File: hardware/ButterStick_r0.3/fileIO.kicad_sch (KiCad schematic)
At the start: 2 parts, among them J4 MicroSD, U20 PUSB3FR6

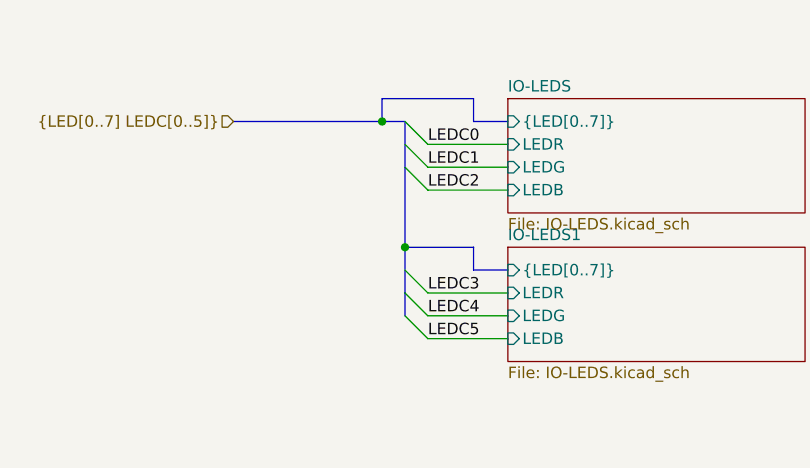
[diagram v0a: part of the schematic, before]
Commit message: hw.r0_3: routing improvements
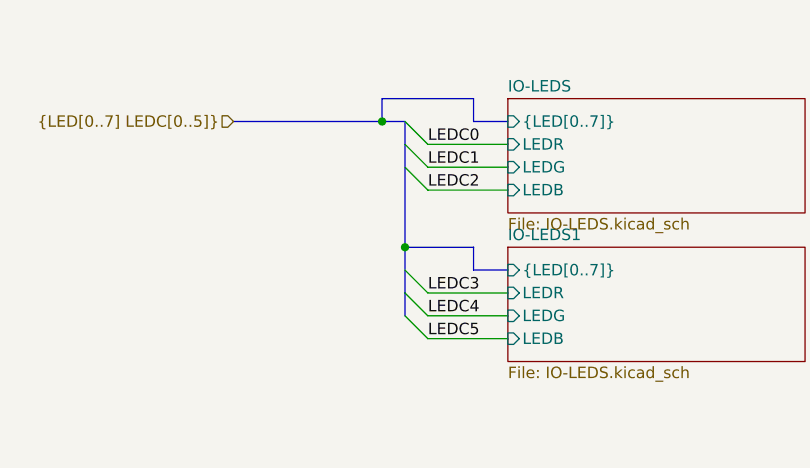
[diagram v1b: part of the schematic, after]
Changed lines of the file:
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@@
 (kicad_sch (version 20200512) (host eeschema "5.99.0-unknown-c8476d6~101~ubuntu18.04.1")
-  (page 4 20)
+  (page 1 20)
   (paper "A4")
   (title_block
@@
   (bus (pts (xy 76.2 40.64) (xy 76.2 38.1)))
   (bus (pts (xy 76.2 40.64) (xy 78.74 40.64)))
-  (bus (pts (xy 78.74 40.64) (xy 78.74 45.72)))
-  (bus (pts (xy 78.74 45.72) (xy 78.74 54.61)))
+  (bus (pts (xy 78.74 40.64) (xy 78.74 43.18)))
+  (bus (pts (xy 78.74 43.18) (xy 78.74 54.61)))
   (bus (pts (xy 78.74 54.61) (xy 78.74 59.69)))
   (bus (pts (xy 78.74 59.69) (xy 78.74 62.23)))

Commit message: hw.r0_3: Start routing DDR3 interface
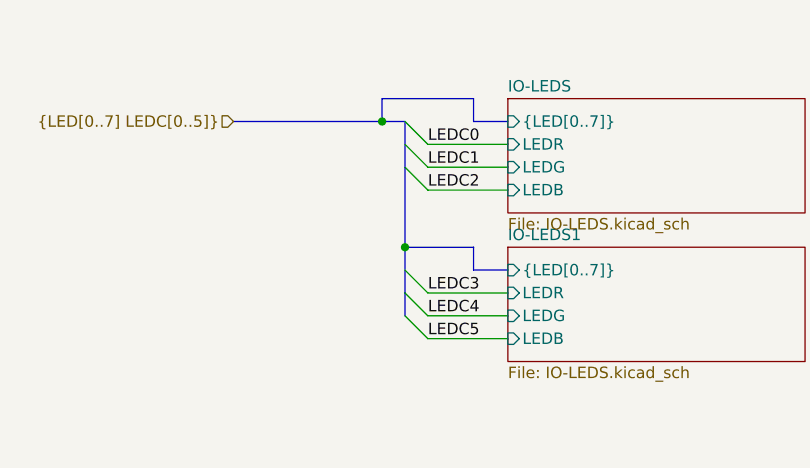
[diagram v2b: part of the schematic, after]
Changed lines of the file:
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@@
-(kicad_sch (version 20200512) (host eeschema "5.99.0-unknown-c8476d6~101~ubuntu18.04.1")
+(kicad_sch (version 20200512) (host eeschema "5.99.0-unknown-711fc99~101~ubuntu18.04.1")
   (page 1 20)
   (paper "A4")
@@
   (bus (pts (xy 76.2 40.64) (xy 76.2 38.1)))
   (bus (pts (xy 76.2 40.64) (xy 78.74 40.64)))
-  (bus (pts (xy 78.74 40.64) (xy 78.74 43.18)))
-  (bus (pts (xy 78.74 43.18) (xy 78.74 54.61)))
+  (bus (pts (xy 78.74 40.64) (xy 78.74 45.72)))
+  (bus (pts (xy 78.74 45.72) (xy 78.74 54.61)))
   (bus (pts (xy 78.74 54.61) (xy 78.74 59.69)))
   (bus (pts (xy 78.74 59.69) (xy 78.74 62.23)))

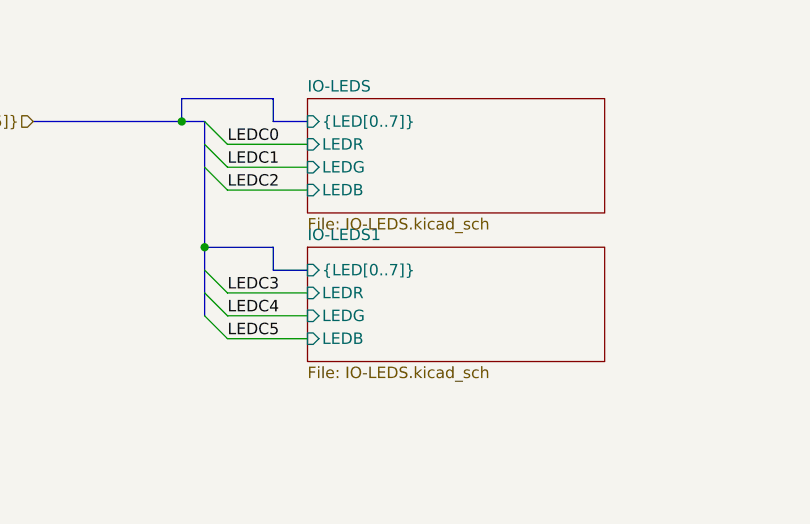
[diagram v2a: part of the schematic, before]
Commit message: hw.r0_3: Inital routing of DDR3 done
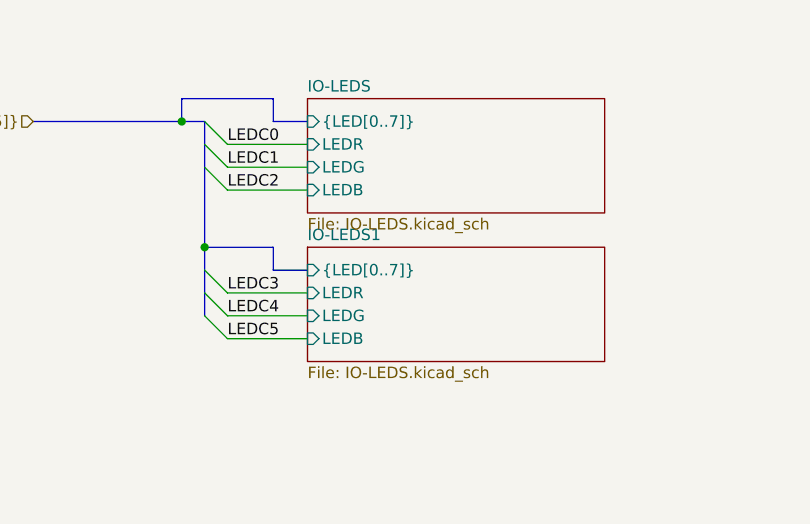
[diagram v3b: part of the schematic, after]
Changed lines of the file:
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@@
   (bus (pts (xy 76.2 40.64) (xy 76.2 38.1)))
   (bus (pts (xy 76.2 40.64) (xy 78.74 40.64)))
-  (bus (pts (xy 78.74 40.64) (xy 78.74 45.72)))
-  (bus (pts (xy 78.74 45.72) (xy 78.74 54.61)))
+  (bus (pts (xy 78.74 40.64) (xy 78.74 43.18)))
+  (bus (pts (xy 78.74 43.18) (xy 78.74 54.61)))
   (bus (pts (xy 78.74 54.61) (xy 78.74 59.69)))
   (bus (pts (xy 78.74 59.69) (xy 78.74 62.23)))
@@
   )
   (sheet (at 90.17 38.1) (size 33.02 12.7)
+    (stroke (width 0.1524) (color 132 0 132 1))
+    (fill (color 255 255 255 1.0000))
     (property "Sheet name" "IO-LEDS" (id 0) (at 90.17 37.4645 0)
       (effects (font (size 1.27 1.27)) (justify left bottom))
@@
   )
   (sheet (at 90.17 54.61) (size 33.02 12.7)
+    (stroke (width 0.1524) (color 132 0 132 1))
+    (fill (color 255 255 255 1.0000))
     (property "Sheet name" "IO-LEDS1" (id 0) (at 90.17 53.9745 0)
       (effects (font (size 1.27 1.27)) (justify left bottom))

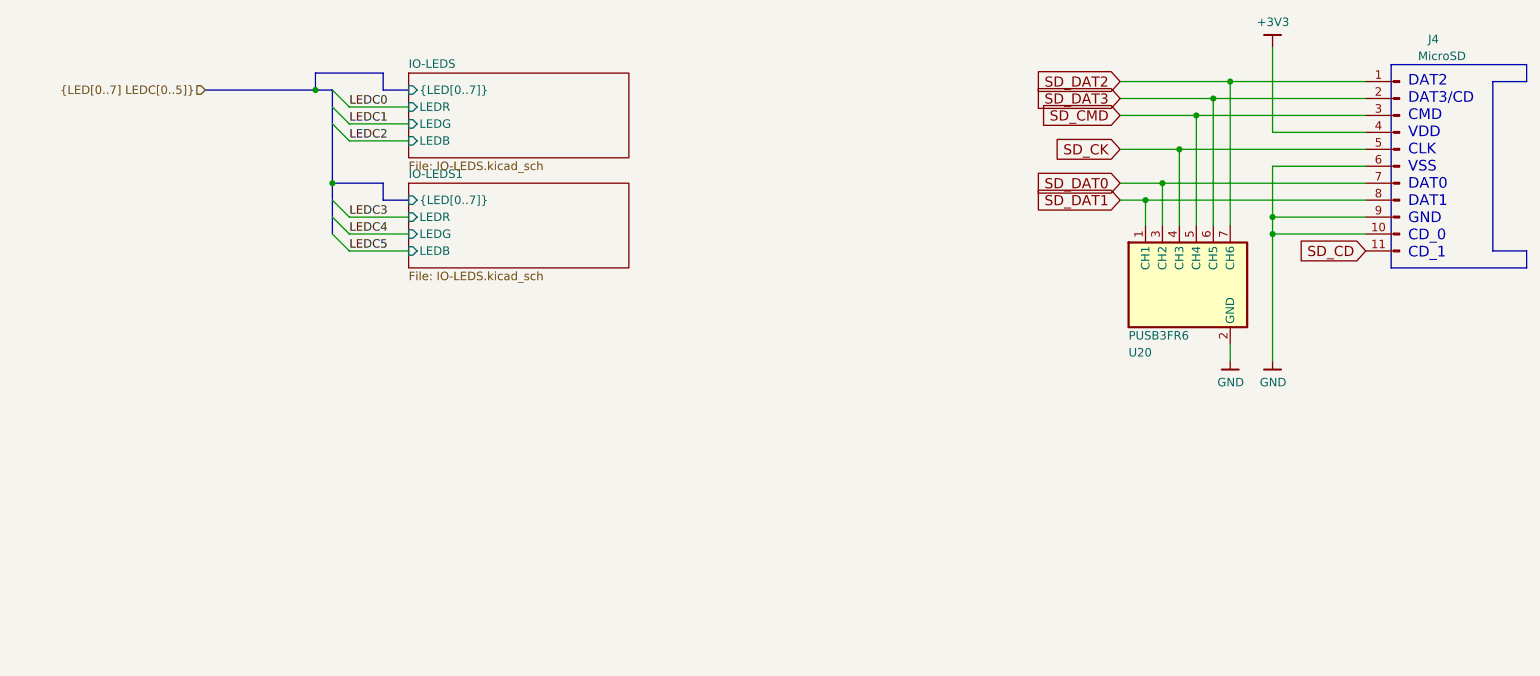
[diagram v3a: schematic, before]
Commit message: hw.r0_3: routed SYZYGY, begin routing RGMII/ULPI
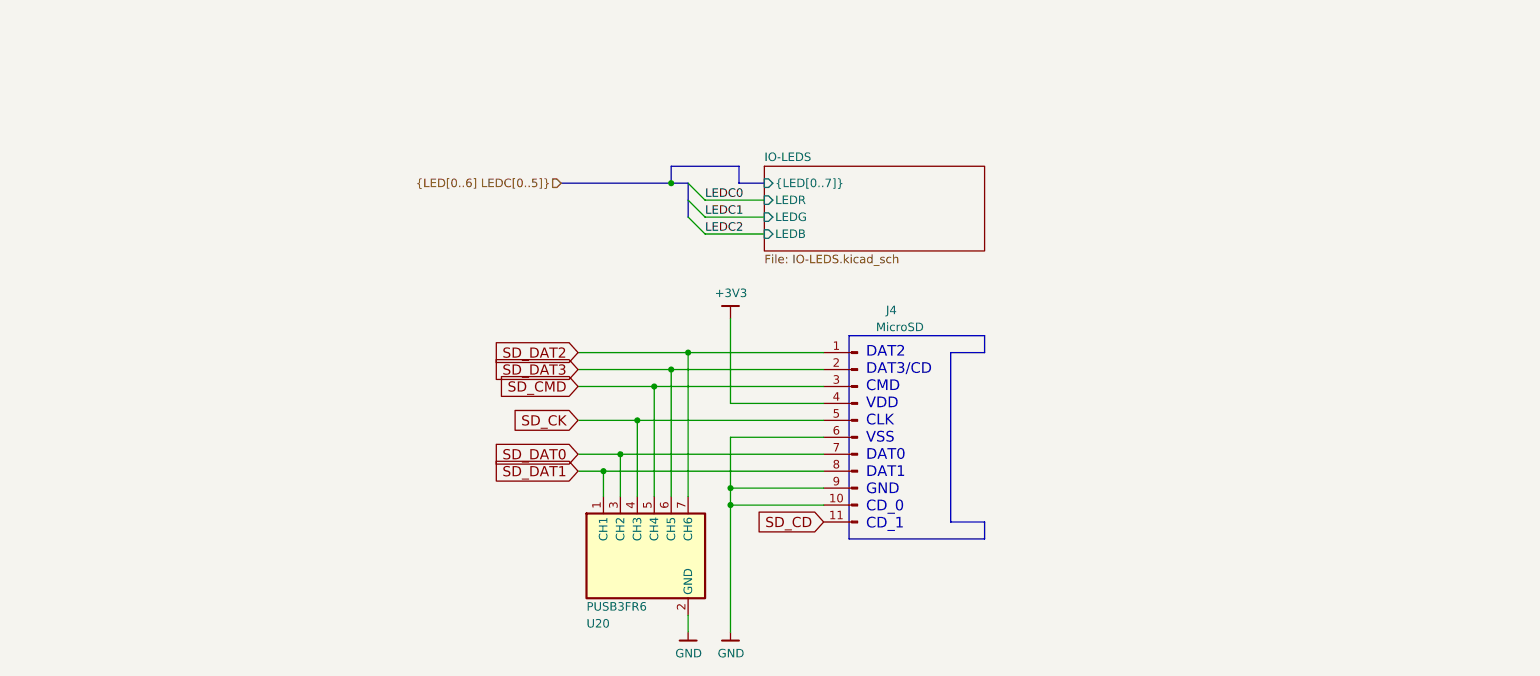
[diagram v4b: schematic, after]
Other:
- removed sheet IO-LEDS1
- moved on the sheet: J4, U20

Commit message: hw.r0_3: major blocks roughly routed
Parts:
- renumbered J4 to J2, U20 to U3
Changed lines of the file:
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@@
   )
   (symbol (lib_id "gkl_power:GND") (at 132.08 121.92 0) (unit 1)
-    (property "Reference" "#PWR0258" (id 0) (at 132.08 128.27 0)
+    (property "Reference" "#PWR054" (id 0) (at 132.08 128.27 0)
       (effects (font (size 1.27 1.27)) hide)
     )
@@
   )
   (symbol (lib_id "gkl_power:GND") (at 138.43 121.92 0) (unit 1)
-    (property "Reference" "#PWR0257" (id 0) (at 138.43 128.27 0)
+    (property "Reference" "#PWR056" (id 0) (at 138.43 128.27 0)
       (effects (font (size 1.27 1.27)) hide)
     )
@@
   )
   (symbol (lib_id "gkl_power:+3V3") (at 138.43 74.93 0) (unit 1)
-    (property "Reference" "#PWR0256" (id 0) (at 138.43 78.74 0)
+    (property "Reference" "#PWR055" (id 0) (at 138.43 78.74 0)
       (effects (font (size 1.27 1.27)) hide)
     )
@@
   )
   (symbol (lib_id "Connector:Conn_01x11_Male") (at 157.48 92.71 0) (mirror y) (unit 1)
-    (property "Reference" "J4" (id 0) (at 162.56 73.66 0))
+    (property "Reference" "J2" (id 0) (at 162.56 73.66 0))
     (property "Value" "MicroSD" (id 1) (at 163.83 76.2 0))
     (property "Footprint" "gkl_conn:molex_microsd_1040310811" (id 2) (at 157.48 92.71 0)
@@
   )
   (symbol (lib_id "gkl_misc:PUSB3FR6") (at 125.73 110.49 90) (mirror x) (unit 1)
-    (property "Reference" "U20" (id 0) (at 116.84 120.65 90)
+    (property "Reference" "U3" (id 0) (at 116.84 120.65 90)
       (effects (font (size 1.27 1.27)) (justify right))
     )

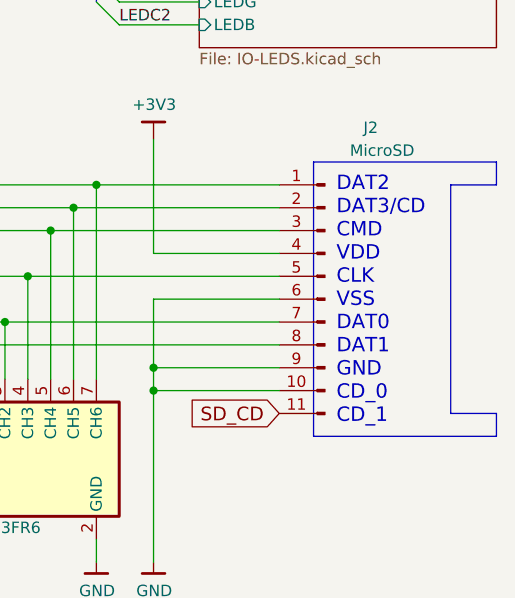
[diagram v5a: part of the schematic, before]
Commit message: hw.r0d3: Length matched all SYZYGY ports
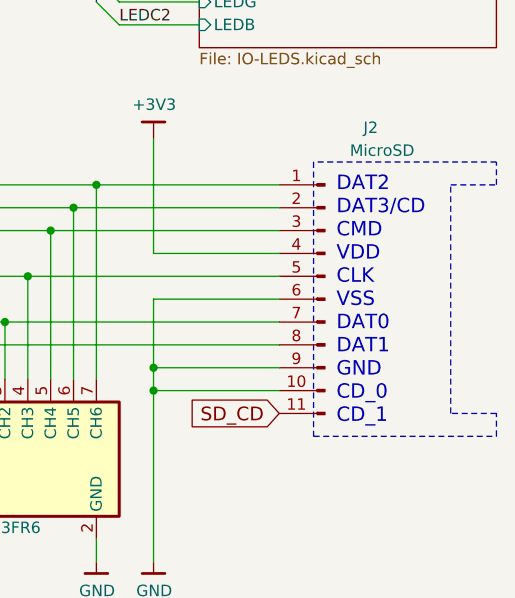
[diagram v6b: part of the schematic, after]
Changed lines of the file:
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@@
-(kicad_sch (version 20200512) (host eeschema "5.99.0-unknown-711fc99~101~ubuntu18.04.1")
+(kicad_sch (version 20200608) (host eeschema "5.99.0-unknown-08c61e6~101~ubuntu18.04.1")
   (page 1 19)
   (paper "A4")
@@
   (bus_entry (at 134.62 59.69) (size -2.54 -2.54))
   (bus_entry (at 134.62 62.23) (size -2.54 -2.54))
-  (wire (pts (xy 115.57 80.01) (xy 132.08 80.01)))
-  (wire (pts (xy 115.57 82.55) (xy 129.54 82.55)))
-  (wire (pts (xy 115.57 85.09) (xy 127 85.09)))
-  (wire (pts (xy 115.57 90.17) (xy 124.46 90.17)))
-  (wire (pts (xy 115.57 95.25) (xy 121.92 95.25)))
-  (wire (pts (xy 115.57 97.79) (xy 119.38 97.79)))
-  (wire (pts (xy 119.38 97.79) (xy 152.4 97.79)))
-  (wire (pts (xy 119.38 101.6) (xy 119.38 97.79)))
-  (wire (pts (xy 121.92 95.25) (xy 152.4 95.25)))
-  (wire (pts (xy 121.92 101.6) (xy 121.92 95.25)))
-  (wire (pts (xy 124.46 90.17) (xy 152.4 90.17)))
-  (wire (pts (xy 124.46 101.6) (xy 124.46 90.17)))
-  (wire (pts (xy 127 85.09) (xy 152.4 85.09)))
-  (wire (pts (xy 127 101.6) (xy 127 85.09)))
-  (wire (pts (xy 129.54 82.55) (xy 152.4 82.55)))
-  (wire (pts (xy 129.54 101.6) (xy 129.54 82.55)))
-  (wire (pts (xy 132.08 80.01) (xy 152.4 80.01)))
-  (wire (pts (xy 132.08 101.6) (xy 132.08 80.01)))
-  (wire (pts (xy 132.08 119.38) (xy 132.08 121.92)))
-  (wire (pts (xy 134.62 57.15) (xy 143.51 57.15)))
-  (wire (pts (xy 134.62 59.69) (xy 143.51 59.69)))
-  (wire (pts (xy 134.62 62.23) (xy 143.51 62.23)))
-  (wire (pts (xy 138.43 87.63) (xy 138.43 74.93)))
-  (wire (pts (xy 138.43 92.71) (xy 138.43 100.33)))
-  (wire (pts (xy 138.43 100.33) (xy 138.43 102.87)))
-  (wire (pts (xy 138.43 100.33) (xy 152.4 100.33)))
-  (wire (pts (xy 138.43 102.87) (xy 138.43 121.92)))
-  (wire (pts (xy 152.4 87.63) (xy 138.43 87.63)))
-  (wire (pts (xy 152.4 92.71) (xy 138.43 92.71)))
-  (wire (pts (xy 152.4 102.87) (xy 138.43 102.87)))
-  (bus (pts (xy 113.03 54.61) (xy 129.54 54.61)))
-  (bus (pts (xy 129.54 52.07) (xy 139.7 52.07)))
-  (bus (pts (xy 129.54 54.61) (xy 129.54 52.07)))
-  (bus (pts (xy 129.54 54.61) (xy 132.08 54.61)))
-  (bus (pts (xy 132.08 54.61) (xy 132.08 59.69)))
-  (bus (pts (xy 139.7 52.07) (xy 139.7 54.61)))
-  (bus (pts (xy 139.7 54.61) (xy 143.51 54.61)))
-  (polyline (pts (xy 156.21 77.47) (xy 156.21 107.95)))
-  (polyline (pts (xy 156.21 107.95) (xy 176.53 107.95)))
-  (polyline (pts (xy 171.45 80.01) (xy 176.53 80.01)))
-  (polyline (pts (xy 171.45 105.41) (xy 171.45 80.01)))
-  (polyline (pts (xy 176.53 77.47) (xy 156.21 77.47)))
-  (polyline (pts (xy 176.53 80.01) (xy 176.53 77.47)))
-  (polyline (pts (xy 176.53 105.41) (xy 171.45 105.41)))
-  (polyline (pts (xy 176.53 107.95) (xy 176.53 105.41)))
+  (wire (pts (xy 115.57 80.01) (xy 132.08 80.01))
+    (stroke (width 0) (type solid) (color 0 0 0 0))
+  )
+  (wire (pts (xy 115.57 82.55) (xy 129.54 82.55))
+    (stroke (width 0) (type solid) (color 0 0 0 0))
+  )
+  (wire (pts (xy 115.57 85.09) (xy 127 85.09))
+    (stroke (width 0) (type solid) (color 0 0 0 0))
+  )
+  (wire (pts (xy 115.57 90.17) (xy 124.46 90.17))
+    (stroke (width 0) (type solid) (color 0 0 0 0))
+  )
+  (wire (pts (xy 115.57 95.25) (xy 121.92 95.25))
+    (stroke (width 0) (type solid) (color 0 0 0 0))
+  )
+  (wire (pts (xy 115.57 97.79) (xy 119.38 97.79))
+    (stroke (width 0) (type solid) (color 0 0 0 0))
+  )
+  (wire (pts (xy 119.38 97.79) (xy 152.4 97.79))
+    (stroke (width 0) (type solid) (color 0 0 0 0))
+  )
+  (wire (pts (xy 119.38 101.6) (xy 119.38 97.79))
+    (stroke (width 0) (type solid) (color 0 0 0 0))
+  )
+  (wire (pts (xy 121.92 95.25) (xy 152.4 95.25))
+    (stroke (width 0) (type solid) (color 0 0 0 0))
+  )
+  (wire (pts (xy 121.92 101.6) (xy 121.92 95.25))
+    (stroke (width 0) (type solid) (color 0 0 0 0))
+  )
+  (wire (pts (xy 124.46 90.17) (xy 152.4 90.17))
+    (stroke (width 0) (type solid) (color 0 0 0 0))
+  )
+  (wire (pts (xy 124.46 101.6) (xy 124.46 90.17))
+    (stroke (width 0) (type solid) (color 0 0 0 0))
+  )
+  (wire (pts (xy 127 85.09) (xy 152.4 85.09))
+    (stroke (width 0) (type solid) (color 0 0 0 0))
+  )
+  (wire (pts (xy 127 101.6) (xy 127 85.09))
+    (stroke (width 0) (type solid) (color 0 0 0 0))
+  )
+  (wire (pts (xy 129.54 82.55) (xy 152.4 82.55))
+    (stroke (width 0) (type solid) (color 0 0 0 0))
+  )
+  (wire (pts (xy 129.54 101.6) (xy 129.54 82.55))
+    (stroke (width 0) (type solid) (color 0 0 0 0))
+  )
+  (wire (pts (xy 132.08 80.01) (xy 152.4 80.01))
+    (stroke (width 0) (type solid) (color 0 0 0 0))
+  )
+  (wire (pts (xy 132.08 101.6) (xy 132.08 80.01))
+    (stroke (width 0) (type solid) (color 0 0 0 0))
+  )
+  (wire (pts (xy 132.08 119.38) (xy 132.08 121.92))
+    (stroke (width 0) (type solid) (color 0 0 0 0))
+  )
+  (wire (pts (xy 134.62 57.15) (xy 143.51 57.15))
+    (stroke (width 0) (type solid) (color 0 0 0 0))
+  )
+  (wire (pts (xy 134.62 59.69) (xy 143.51 59.69))
+    (stroke (width 0) (type solid) (color 0 0 0 0))
+  )
+  (wire (pts (xy 134.62 62.23) (xy 143.51 62.23))
+    (stroke (width 0) (type solid) (color 0 0 0 0))
+  )
+  (wire (pts (xy 138.43 87.63) (xy 138.43 74.93))
+    (stroke (width 0) (type solid) (color 0 0 0 0))
+  )
+  (wire (pts (xy 138.43 92.71) (xy 138.43 100.33))
+    (stroke (width 0) (type solid) (color 0 0 0 0))
+  )
+  (wire (pts (xy 138.43 100.33) (xy 138.43 102.87))
+    (stroke (width 0) (type solid) (color 0 0 0 0))
+  )
+  (wire (pts (xy 138.43 100.33) (xy 152.4 100.33))
+    (stroke (width 0) (type solid) (color 0 0 0 0))
+  )
+  (wire (pts (xy 138.43 102.87) (xy 138.43 121.92))
+    (stroke (width 0) (type solid) (color 0 0 0 0))
+  )
+  (wire (pts (xy 152.4 87.63) (xy 138.43 87.63))
+    (stroke (width 0) (type solid) (color 0 0 0 0))
+  )
+  (wire (pts (xy 152.4 92.71) (xy 138.43 92.71))
+    (stroke (width 0) (type solid) (color 0 0 0 0))
+  )
+  (wire (pts (xy 152.4 102.87) (xy 138.43 102.87))
+    (stroke (width 0) (type solid) (color 0 0 0 0))
+  )
+  (bus (pts (xy 113.03 54.61) (xy 129.54 54.61))
+    (stroke (width 0) (type solid) (color 0 0 0 0))
+  )
+  (bus (pts (xy 129.54 52.07) (xy 139.7 52.07))
+    (stroke (width 0) (type solid) (color 0 0 0 0))
+  )
+  (bus (pts (xy 129.54 54.61) (xy 129.54 52.07))
+    (stroke (width 0) (type solid) (color 0 0 0 0))
+  )
+  (bus (pts (xy 129.54 54.61) (xy 132.08 54.61))
+    (stroke (width 0) (type solid) (color 0 0 0 0))
+  )
+  (bus (pts (xy 132.08 54.61) (xy 132.08 59.69))
+    (stroke (width 0) (type solid) (color 0 0 0 0))
+  )
+  (bus (pts (xy 139.7 52.07) (xy 139.7 54.61))
+    (stroke (width 0) (type solid) (color 0 0 0 0))
+  )
+  (bus (pts (xy 139.7 54.61) (xy 143.51 54.61))
+    (stroke (width 0) (type solid) (color 0 0 0 0))
+  )
+  (polyline (pts (xy 156.21 77.47) (xy 156.21 107.95))
+    (stroke (width 0) (type dash) (color 0 0 0 0))
+  )
+  (polyline (pts (xy 156.21 107.95) (xy 176.53 107.95))
+    (stroke (width 0) (type dash) (color 0 0 0 0))
+  )
+  (polyline (pts (xy 171.45 80.01) (xy 176.53 80.01))
+    (stroke (width 0) (type dash) (color 0 0 0 0))
+  )
+  (polyline (pts (xy 171.45 105.41) (xy 171.45 80.01))
+    (stroke (width 0) (type dash) (color 0 0 0 0))
+  )
+  (polyline (pts (xy 176.53 77.47) (xy 156.21 77.47))
+    (stroke (width 0) (type dash) (color 0 0 0 0))
+  )
+  (polyline (pts (xy 176.53 80.01) (xy 176.53 77.47))
+    (stroke (width 0) (type dash) (color 0 0 0 0))
+  )
+  (polyline (pts (xy 176.53 105.41) (xy 171.45 105.41))
+    (stroke (width 0) (type dash) (color 0 0 0 0))
+  )
+  (polyline (pts (xy 176.53 107.95) (xy 176.53 105.41))
+    (stroke (width 0) (type dash) (color 0 0 0 0))
+  )
   (text "DAT2\nDAT3/CD\nCMD\nVDD\nCLK\nVSS\nDAT0\nDAT1\nGND\nCD_0\nCD_1\n"
     (at 158.75 106.68 0)
@@
   )
   (symbol (lib_id "gkl_power:GND") (at 132.08 121.92 0) (unit 1)
-    (property "Reference" "#PWR054" (id 0) (at 132.08 128.27 0)
+    (in_bom yes) (on_board yes)
+    (property "Reference" "#PWR055" (id 0) (at 132.08 128.27 0)
       (effects (font (size 1.27 1.27)) hide)
     )
@@
   )
   (symbol (lib_id "gkl_power:GND") (at 138.43 121.92 0) (unit 1)
-    (property "Reference" "#PWR056" (id 0) (at 138.43 128.27 0)
+    (in_bom yes) (on_board yes)
+    (property "Reference" "#PWR057" (id 0) (at 138.43 128.27 0)
       (effects (font (size 1.27 1.27)) hide)
     )
@@
   )
   (symbol (lib_id "gkl_power:+3V3") (at 138.43 74.93 0) (unit 1)
-    (property "Reference" "#PWR055" (id 0) (at 138.43 78.74 0)
+    (in_bom yes) (on_board yes)
+    (property "Reference" "#PWR056" (id 0) (at 138.43 78.74 0)
       (effects (font (size 1.27 1.27)) hide)
     )
@@
   )
   (symbol (lib_id "Connector:Conn_01x11_Male") (at 157.48 92.71 0) (mirror y) (unit 1)
+    (in_bom yes) (on_board yes)
     (property "Reference" "J2" (id 0) (at 162.56 73.66 0))
     (property "Value" "MicroSD" (id 1) (at 163.83 76.2 0))
@@
   )
   (symbol (lib_id "gkl_misc:PUSB3FR6") (at 125.73 110.49 90) (mirror x) (unit 1)
+    (in_bom yes) (on_board yes)
     (property "Reference" "U3" (id 0) (at 116.84 120.65 90)
       (effects (font (size 1.27 1.27)) (justify right))
@@
   )
   (sheet (at 143.51 52.07) (size 33.02 12.7)
-    (stroke (width 0.1524) (color 132 0 132 1))
+    (stroke (width 0.1524) (type solid) (color 132 0 132 1))
     (fill (color 255 255 255 1.0000))
     (property "Sheet name" "IO-LEDS" (id 0) (at 143.51 51.4345 0)
